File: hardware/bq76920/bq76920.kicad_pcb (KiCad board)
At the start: 2 copper layers, 80 x 40 mm, 86 parts, among them J1 BAT+, J2 Conn_01x06, J3 therm, J4 boot_switch, J5 BAT-, J6 PACK+, J7 PACK-, J8 mcu interface, Q1 PSMN2R6-40YS, Q2 SI2337DS-T1-E3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

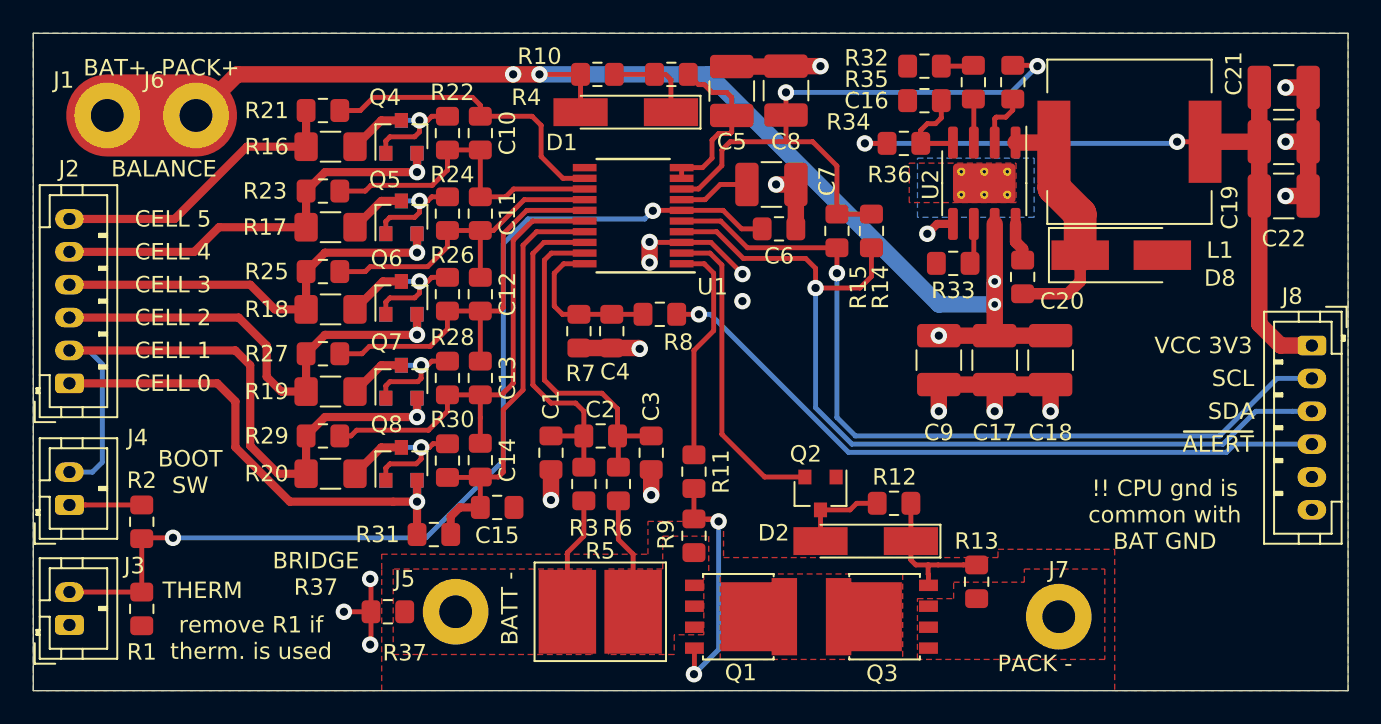
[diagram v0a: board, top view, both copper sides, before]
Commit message: clean up, adnotate, footprints
Signed-off-by: Ene Alexandru <ene.alexandru@gmail.com>
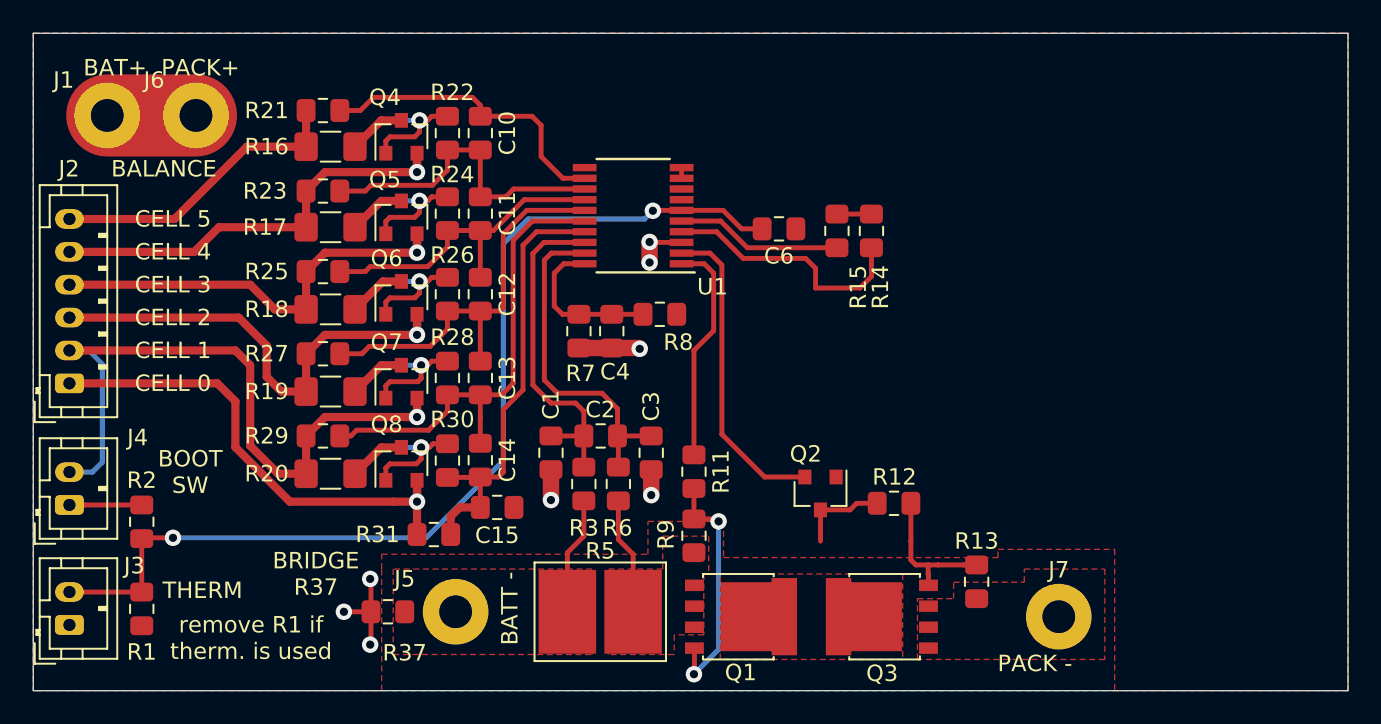
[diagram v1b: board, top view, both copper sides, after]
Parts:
- removed C16: 680p, Capacitor_SMD:C_0805_2012Metric_Pad1.15x1.40mm_HandSolder
- removed C17, C18, C19, C21, C22, C5, C7, C8, C9: 12105C106KAT2A, Capacitor_SMD:C_1210_3225Metric_Pad1.42x2.65mm_HandSolder
- removed C20: 100n, Capacitor_SMD:C_0805_2012Metric_Pad1.15x1.40mm_HandSolder
- removed D1, D2: LL4148-GS08, Diode_SMD:D_MiniMELF_Handsoldering
- removed D3, D4, D5, D6, D7: BZX84C5V6LT3G, Package_TO_SOT_SMD:SOT-23
- removed D8: CMSH2-100M TR13, Diode_SMD:D_SMA_Handsoldering
- removed J8: mcu interface, Connector_JST:JST_PH_B6B-PH-K_1x06_P2.00mm_Vertical
- removed L1: 744066100, bq76920:744066100
- removed R10: 100, Resistor_SMD:R_0805_2012Metric_Pad1.15x1.40mm_HandSolder
- removed R32: 100k, Resistor_SMD:R_0805_2012Metric_Pad1.15x1.40mm_HandSolder
- removed R33: 200k, Resistor_SMD:R_0805_2012Metric_Pad1.15x1.40mm_HandSolder
- removed R34: 40.2k, Resistor_SMD:R_0805_2012Metric_Pad1.15x1.40mm_HandSolder
- removed R35: 24k, Resistor_SMD:R_0805_2012Metric_Pad1.15x1.40mm_HandSolder
- removed R36: 127k, Resistor_SMD:R_0805_2012Metric_Pad1.15x1.40mm_HandSolder
- removed R4: 10k, Resistor_SMD:R_0805_2012Metric_Pad1.15x1.40mm_HandSolder
- removed U2: MP4559, Package_SO:SOIC-8-1EP_3.9x4.9mm_P1.27mm_EP2.41x3.81mm_ThermalVias
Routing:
- net /BAT+: track 80.6 -> 5.40 mm, vias 5 -> 0
- net /VCC_3V3: track 43.5 -> 0.00 mm, vias 2 -> 0
- net /~ALERT: track 42.3 -> 0.00 mm, vias 1 -> 0
- net /SCL: track 51.3 -> 10.1 mm, vias 1 -> 0
- net /SDA: track 54.9 -> 15.7 mm, vias 1 -> 0
- net GND: track 55.7 -> 17.7 mm, vias 19 -> 8
- net /cpu power/ENABLE: track 37.3 -> 2.10 mm, vias 2 -> 0
- net Net-(C20-Pad1): track 15.3 -> 0.00 mm
- net Net-(C5-Pad2): track 10.6 -> 0.65 mm
- net Net-(D1-Pad1): track 5.56 -> 0.00 mm
- net Net-(R34-Pad1): track 5.39 -> 0.00 mm
- net Net-(C7-Pad2): track 4.36 -> 0.00 mm
- net Net-(R32-Pad1): track 3.44 -> 0.00 mm
- net Net-(R35-Pad1): track 2.66 -> 0.00 mm
- net Net-(R33-Pad1): track 2.50 -> 0.00 mm
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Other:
- board text removed: "!! CPU gnd is common with BAT GND"
- board text removed: "SCL"
- board text removed: "SDA"
- board text removed: "VCC 3V3"
- board text removed: "~ALERT"
